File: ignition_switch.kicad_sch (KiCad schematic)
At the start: 6 parts, among them U11 EL3H7, U9 EL3H7

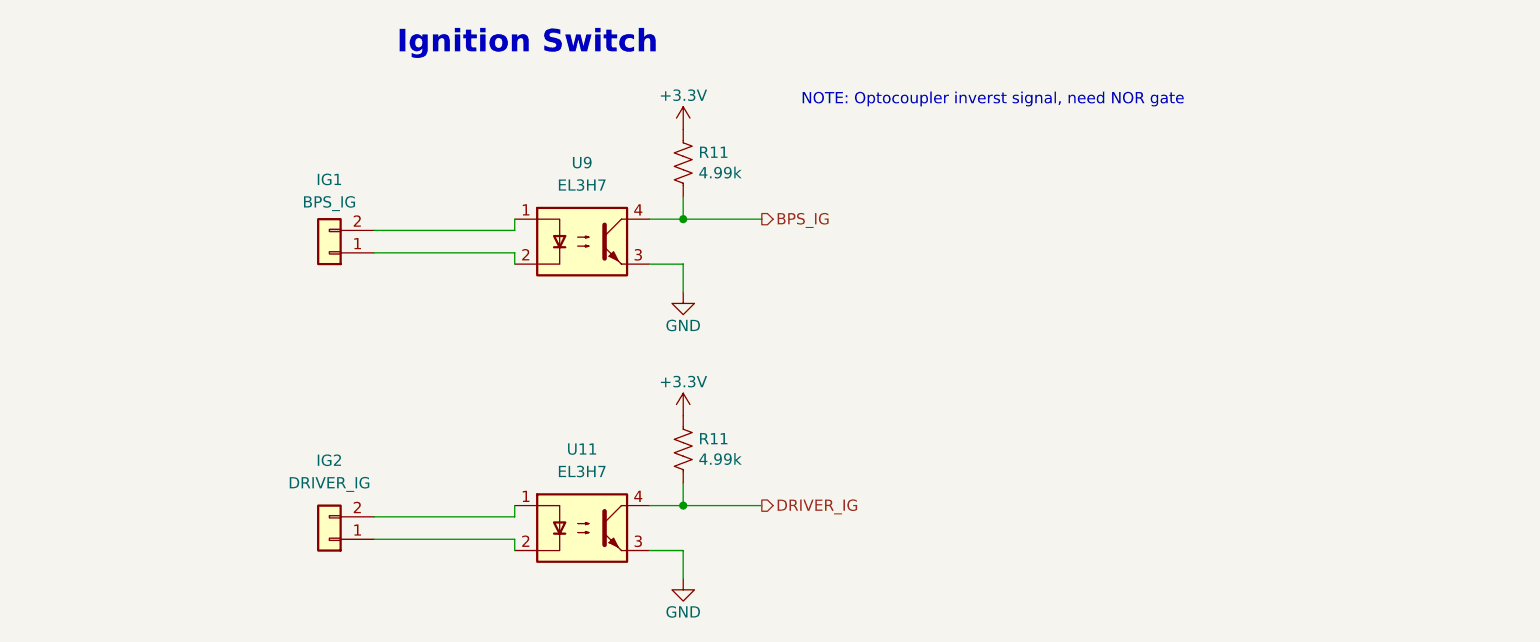
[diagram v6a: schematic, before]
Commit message: Added test points
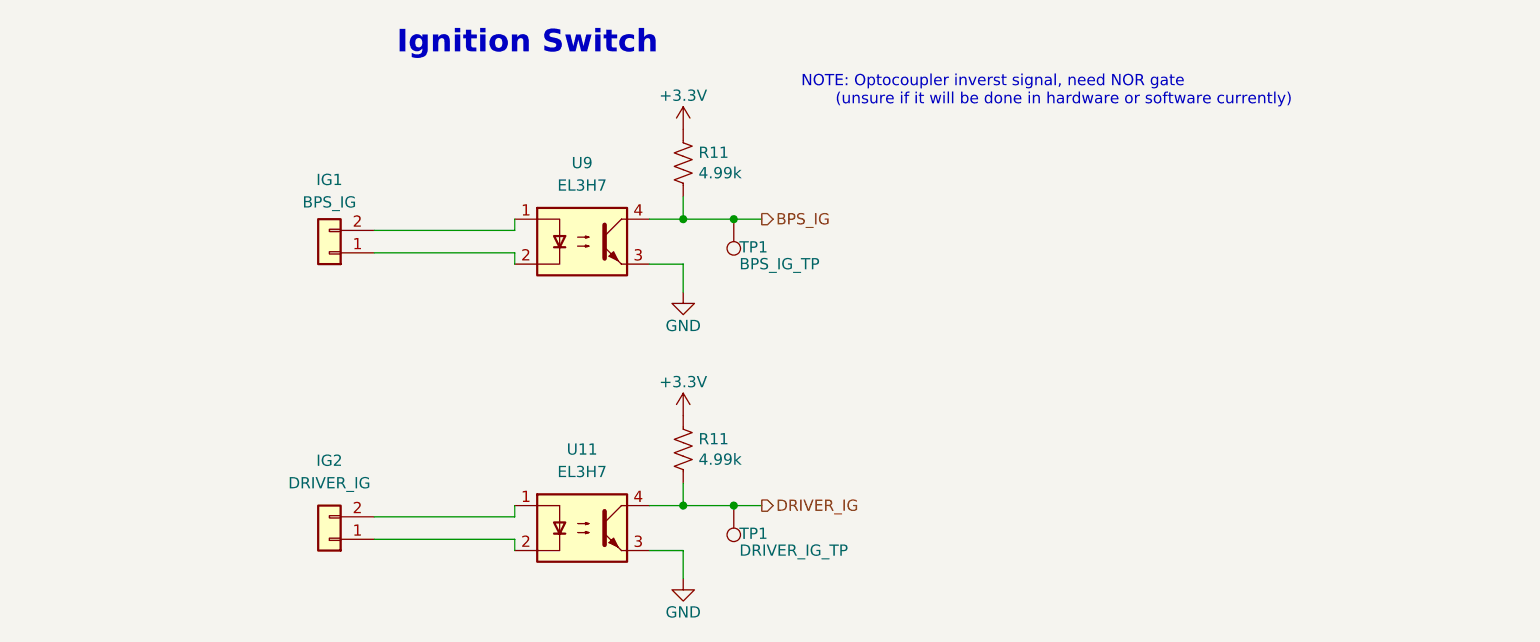
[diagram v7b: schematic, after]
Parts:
- added TP1: DRIVER_IG_TP, symbol Connector:TestPoint
- added TP1: BPS_IG_TP, symbol Connector:TestPoint
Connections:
- net BPS_IG: now also TP1.1
- net DRIVER_IG: now also TP1.1
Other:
- note added: "NOTE: Optocoupler inverst signal, need NOR gate (unsure if it will be done in hardware or software currently)"
- note removed: "NOTE: Optocoupler inverst signal, need NOR gate"
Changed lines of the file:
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@@
   (junction (at 147.955 105.41) (diameter 0) (color 0 0 0 0)
   )
+  (junction (at 153.67 73.025) (diameter 0) (color 0 0 0 0)
+  )
+  (junction (at 153.67 105.41) (diameter 0) (color 0 0 0 0)
+  )
   (junction (at 147.955 73.025) (diameter 0) (color 0 0 0 0)
   )
@@
     (stroke (width 0) (type default))
   )
-  (wire (pts (xy 147.955 73.025) (xy 156.845 73.025))
+  (wire (pts (xy 147.955 73.025) (xy 153.67 73.025))
     (stroke (width 0) (type default))
   )
@@
     (stroke (width 0) (type default))
   )
-  (wire (pts (xy 147.955 105.41) (xy 156.845 105.41))
+  (wire (pts (xy 147.955 105.41) (xy 153.67 105.41))
     (stroke (width 0) (type default))
   )
@@
     (stroke (width 0) (type default))
   )
+  (wire (pts (xy 153.67 105.41) (xy 156.845 105.41))
+    (stroke (width 0) (type default))
+  )
   (wire (pts (xy 147.955 70.485) (xy 147.955 73.025))
+    (stroke (width 0) (type default))
+  )
+  (wire (pts (xy 153.67 73.025) (xy 156.845 73.025))
     (stroke (width 0) (type default))
   )
@@
     (effects (font (size 2.54 2.54) (thickness 0.508) bold) (justify left bottom))
   )
-  (text "NOTE: Optocoupler inverst signal, need NOR gate" (at 161.29 60.325 0)
+  (text "NOTE: Optocoupler inverst signal, need NOR gate \n       (unsure if it will be done in hardware or software currently)"
+    (at 161.29 60.325 0)
     (effects (font (size 1.27 1.27)) (justify left bottom))
   )
@@
     )
   )
+  (symbol (lib_id "Connector:TestPoint") (at 153.67 105.41 180) (unit 1)
+    (in_bom yes) (on_board yes) (dnp no)
+    (property "Reference" "TP1" (at 154.305 108.585 0)
+      (effects (font (size 1.27 1.27)) (justify right))
+    )
+    (property "Value" "DRIVER_IG_TP" (at 154.305 110.49 0)
+      (effects (font (size 1.27 1.27)) (justify right))
+    )
+    (property "Footprint" "" (at 148.59 105.41 0)
+      (effects (font (size 1.27 1.27)) hide)
+    )
+    (property "Datasheet" "~" (at 148.59 105.41 0)
+      (effects (font (size 1.27 1.27)) hide)
+    )
+    (pin "1")
+    (instances
+      (project "Controls-LeaderDaughterPCB"
+        (path "/c7871779-04fe-4705-8150-20a4dd0ef44f"
+          (reference "TP1") (unit 1)
+        )
+        (path "/c7871779-04fe-4705-8150-20a4dd0ef44f/52d17704-1dcb-4587-b732-713a215b01d3"
+          (reference "TP13") (unit 1)
+        )
+        (path "/c7871779-04fe-4705-8150-20a4dd0ef44f/0d7b9330-5178-458e-b803-9c8d464fd559"
+          (reference "TP16") (unit 1)
+        )
+      )
+    )
+  )
   (symbol (lib_id "Device:R_US") (at 147.955 66.675 0) (unit 1)
     (in_bom yes) (on_board yes) (dnp no)
@@
         )
       )
+    )
+  )
+  (symbol (lib_id "Connector:TestPoint") (at 153.67 73.025 180) (unit 1)
+    (in_bom yes) (on_board yes) (dnp no)
+    (property "Reference" "TP1" (at 154.305 76.2 0)
+      (effects (font (size 1.27 1.27)) (justify right))
+    )
+    (property "Value" "BPS_IG_TP" (at 154.305 78.105 0)
+      (effects (font (size 1.27 1.27)) (justify right))
+    )
+    (property "Footprint" "" (at 148.59 73.025 0)
+      (effects (font (size 1.27 1.27)) hide)
+    )
+    (property "Datasheet" "~" (at 148.59 73.025 0)
+      (effects (font (size 1.27 1.27)) hide)
+    )
+    (pin "1")
+    (instances
+      (project "Controls-LeaderDaughterPCB"
+        (path "/c7871779-04fe-4705-8150-20a4dd0ef44f"
+          (reference "TP1") (unit 1)
+        )
+        (path "/c7871779-04fe-4705-8150-20a4dd0ef44f/52d17704-1dcb-4587-b732-713a215b01d3"
+          (reference "TP13") (unit 1)
+        )
+        (path "/c7871779-04fe-4705-8150-20a4dd0ef44f/0d7b9330-5178-458e-b803-9c8d464fd559"
+          (reference "TP15") (unit 1)
+        )
+      )

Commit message: Adjusted & added footprints, several minor changes
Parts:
- TP1: footprint (none) -> TestPoint:TestPoint_Pad_1.5x1.5mm
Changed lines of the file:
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@@
       (effects (font (size 1.27 1.27)) (justify right))
     )
-    (property "Footprint" "" (at 148.59 105.41 0)
+    (property "Footprint" "TestPoint:TestPoint_Pad_1.5x1.5mm" (at 148.59 105.41 0)
       (effects (font (size 1.27 1.27)) hide)
     )
@@
       (effects (font (size 1.27 1.27)) (justify right))
     )
-    (property "Footprint" "" (at 148.59 73.025 0)
+    (property "Footprint" "TestPoint:TestPoint_Pad_1.5x1.5mm" (at 148.59 73.025 0)
       (effects (font (size 1.27 1.27)) hide)
     )
